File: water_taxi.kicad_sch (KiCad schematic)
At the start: 28 parts

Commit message: pier 50 routing checkpoint
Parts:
- removed LED538, LED587: WS2812B-2020, EasyEDA:LED-SMD_4P-L2.0-W2.0-TL_WS2812B-2020, symbol EasyEDA:WS2812B-2020
- added LED596, LED597, LED598, LED599: WS2812B-2020, EasyEDA:LED-SMD_4P-L2.0-W2.0-TL_WS2812B-2020, symbol EasyEDA:WS2812B-2020
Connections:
- net +VLED: now also LED596.4 (VDD), LED597.4 (VDD), LED598.4 (VDD), LED599.4 (VDD)
- net GND: now also LED596.2 (GND), LED597.2 (GND), LED598.2 (GND), LED599.2 (GND)
- net at LED539.3 (DI): now also LED537.1 (DO)
- net at LED588.3 (DI): now also LED586.1 (DO)
- net at LED593.1 (DO): now also LED598.3 (DI)
- net at LED593.3 (DI): now also LED599.1 (DO); no longer LED591.1 (DO)
- net at LED532.3 (DI): now also LED596.1 (DO)
- net at LED594.1 (DO): now also LED597.3 (DI)
- new net: LED591.1 (DO), LED599.3 (DI)
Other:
- moved on the sheet: LED532, LED534, LED535, LED536, LED537, LED539, LED540, LED541, LED542, LED543, LED544, LED545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

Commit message: single ferry track checkpoint
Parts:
- removed LED582, LED583, LED584, LED585, LED586, LED588, LED589, LED590, LED591, LED592, LED593, LED594, LED597, LED598, LED599: WS2812B-2020, EasyEDA:LED-SMD_4P-L2.0-W2.0-TL_WS2812B-2020, symbol EasyEDA:WS2812B-2020
- added LED538, LED553: WS2812B-2020, EasyEDA:LED-SMD_4P-L2.0-W2.0-TL_WS2812B-2020, symbol EasyEDA:WS2812B-2020
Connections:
- net +VLED: now also LED538.4 (VDD), LED553.4 (VDD)
- net GND: now also LED538.2 (GND), LED553.2 (GND)
- net at LED545.1 (DO): now also LED553.3 (DI); no longer LED546.3 (DI)
- net at LED534.3 (DI): now also LED538.1 (DO); no longer LED532.1 (DO)
- new net: LED546.3 (DI), LED553.1 (DO)
- new net: LED532.1 (DO), LED538.3 (DI)
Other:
- moved on the sheet: LED534, LED535, LED536, LED537

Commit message: checkpoint before label plugin
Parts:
- added LED554: WS2812B-2020, EasyEDA:LED-SMD_4P-L2.0-W2.0-TL_WS2812B-2020, symbol EasyEDA:WS2812B-2020
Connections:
- net +VLED: now also LED554.4 (VDD)
- net GND: now also LED554.2 (GND)
- net at LED544.4 (DIN): now also LED554.1 (DO); no longer LED543.1 (DO)
- new net: LED543.1 (DO), LED554.3 (DI)

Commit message: Add rail labels
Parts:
- renumbered LED596 to LED501, LED532 to LED502, LED538 to LED503, LED534 to LED504, LED535 to LED505, LED536 to LED506, LED537 to LED507, LED539 to LED508, LED540 to LED509, LED541 to LED510, LED542 to LED511, LED543 to LED512, LED554 to LED513, LED544 to LED514, LED545 to LED515, LED553 to LED516, LED546 to LED517, LED547 to LED518
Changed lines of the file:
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@@
 		(in_pos_files yes)
 		(dnp no)
-		(property "Reference" "LED554"
+		(property "Reference" "LED513"
 			(at 267.97 34.544 0)
 			(show_name no)
@@
 			(project "transit"
 				(path "/3763eade-a8c8-4ec0-9cf2-9db4442b4ee5/153adc6e-a3b0-4527-a19a-87e28aab4b4d/f90621d2-7226-466f-89f1-cc8a4ff4cef7"
-					(reference "LED554")
+					(reference "LED513")
 					(unit 1)
 				)
@@
 		(in_pos_files yes)
 		(dnp no)
-		(property "Reference" "LED545"
+		(property "Reference" "LED515"
 			(at 58.42 61.214 0)
 			(show_name no)
@@
 			(project "transit"
 				(path "/3763eade-a8c8-4ec0-9cf2-9db4442b4ee5/153adc6e-a3b0-4527-a19a-87e28aab4b4d/f90621d2-7226-466f-89f1-cc8a4ff4cef7"
-					(reference "LED545")
+					(reference "LED515")
 					(unit 1)
 				)
@@
 		(in_pos_files yes)
 		(dnp no)
-		(property "Reference" "LED546"
+		(property "Reference" "LED517"
 			(at 109.22 61.214 0)
 			(show_name no)
@@
 			(project "transit"
 				(path "/3763eade-a8c8-4ec0-9cf2-9db4442b4ee5/153adc6e-a3b0-4527-a19a-87e28aab4b4d/f90621d2-7226-466f-89f1-cc8a4ff4cef7"
-					(reference "LED546")
+					(reference "LED517")
 					(unit 1)
 				)
@@
 		(in_pos_files yes)
 		(dnp no)
-		(property "Reference" "LED539"
+		(property "Reference" "LED508"
 			(at 170.18 34.544 0)
 			(show_name no)
@@
 			(project "transit"
 				(path "/3763eade-a8c8-4ec0-9cf2-9db4442b4ee5/153adc6e-a3b0-4527-a19a-87e28aab4b4d/f90621d2-7226-466f-89f1-cc8a4ff4cef7"
-					(reference "LED539")
+					(reference "LED508")
 					(unit 1)
 				)
@@
 		(in_pos_files yes)
 		(dnp no)
-		(property "Reference" "LED596"
+		(property "Reference" "LED501"
 			(at 34.29 34.544 0)
 			(show_name no)
@@
 			(project "transit"
 				(path "/3763eade-a8c8-4ec0-9cf2-9db4442b4ee5/153adc6e-a3b0-4527-a19a-87e28aab4b4d/f90621d2-7226-466f-89f1-cc8a4ff4cef7"
-					(reference "LED596")
+					(reference "LED501")
 					(unit 1)
 				)
@@
 		(in_pos_files yes)
 		(dnp no)
-		(property "Reference" "LED534"
+		(property "Reference" "LED504"
 			(at 92.71 34.544 0)
 			(show_name no)
@@
 			(project "transit"
 				(path "/3763eade-a8c8-4ec0-9cf2-9db4442b4ee5/153adc6e-a3b0-4527-a19a-87e28aab4b4d/f90621d2-7226-466f-89f1-cc8a4ff4cef7"
-					(reference "LED534")
+					(reference "LED504")
 					(unit 1)
 				)
@@
 		(in_pos_files yes)
 		(dnp no)
-		(property "Reference" "LED538"
+		(property "Reference" "LED503"
 			(at 73.66 34.544 0)
 			(show_name no)
@@
 			(project "transit"
 				(path "/3763eade-a8c8-4ec0-9cf2-9db4442b4ee5/153adc6e-a3b0-4527-a19a-87e28aab4b4d/f90621d2-7226-466f-89f1-cc8a4ff4cef7"
-					(reference "LED538")
+					(reference "LED503")
 					(unit 1)
 				)
@@
 		(in_pos_files yes)
 		(dnp no)
-		(property "Reference" "LED535"
+		(property "Reference" "LED505"
 			(at 111.76 34.544 0)
 			(show_name no)
@@
 			(project "transit"
 				(path "/3763eade-a8c8-4ec0-9cf2-9db4442b4ee5/153adc6e-a3b0-4527-a19a-87e28aab4b4d/f90621d2-7226-466f-89f1-cc8a4ff4cef7"
-					(reference "LED535")
+					(reference "LED505")
 					(unit 1)
 				)
@@
 		(in_pos_files yes)
 		(dnp no)
-		(property "Reference" "LED536"
+		(property "Reference" "LED506"
 			(at 130.81 34.544 0)
 			(show_name no)
@@
 			(project "transit"
 				(path "/3763eade-a8c8-4ec0-9cf2-9db4442b4ee5/153adc6e-a3b0-4527-a19a-87e28aab4b4d/f90621d2-7226-466f-89f1-cc8a4ff4cef7"
-					(reference "LED536")
+					(reference "LED506")
 					(unit 1)
 				)
@@
 		(in_pos_files yes)
 		(dnp no)
-		(property "Reference" "LED553"
+		(property "Reference" "LED516"
 			(at 82.55 61.214 0)
 			(show_name no)
@@
 			(project "transit"
 				(path "/3763eade-a8c8-4ec0-9cf2-9db4442b4ee5/153adc6e-a3b0-4527-a19a-87e28aab4b4d/f90621d2-7226-466f-89f1-cc8a4ff4cef7"
-					(reference "LED553")
+					(reference "LED516")
 					(unit 1)
 				)
@@
 		(in_pos_files yes)
 		(dnp no)
-		(property "Reference" "LED542"
+		(property "Reference" "LED511"
 			(at 227.33 34.544 0)
 			(show_name no)
@@
 			(project "transit"
 				(path "/3763eade-a8c8-4ec0-9cf2-9db4442b4ee5/153adc6e-a3b0-4527-a19a-87e28aab4b4d/f90621d2-7226-466f-89f1-cc8a4ff4cef7"
-					(reference "LED542")
+					(reference "LED511")
 					(unit 1)
 				)
@@
 		(in_pos_files yes)
 		(dnp no)
-		(property "Reference" "LED544"
+		(property "Reference" "LED514"
 			(at 33.02 58.166 0)
 			(show_name no)
@@
 			(project "transit"
 				(path "/3763eade-a8c8-4ec0-9cf2-9db4442b4ee5/153adc6e-a3b0-4527-a19a-87e28aab4b4d/f90621d2-7226-466f-89f1-cc8a4ff4cef7"
-					(reference "LED544")
+					(reference "LED514")
 					(unit 1)
 				)
@@
 		(in_pos_files yes)
 		(dnp no)
-		(property "Reference" "LED532"
+		(property "Reference" "LED502"
 			(at 54.61 34.544 0)
 			(show_name no)
@@
 			(project "transit"
 				(path "/3763eade-a8c8-4ec0-9cf2-9db4442b4ee5/153adc6e-a3b0-4527-a19a-87e28aab4b4d/f90621d2-7226-466f-89f1-cc8a4ff4cef7"
-					(reference "LED532")
+					(reference "LED502")
 					(unit 1)
 				)
@@
 		(in_pos_files yes)
 		(dnp no)
-		(property "Reference" "LED540"
+		(property "Reference" "LED509"
 			(at 189.23 34.544 0)
 			(show_name no)
@@
 			(project "transit"
 				(path "/3763eade-a8c8-4ec0-9cf2-9db4442b4ee5/153adc6e-a3b0-4527-a19a-87e28aab4b4d/f90621d2-7226-466f-89f1-cc8a4ff4cef7"
-					(reference "LED540")
+					(reference "LED509")
 					(unit 1)
 				)
@@
 		(in_pos_files yes)
 		(dnp no)
-		(property "Reference" "LED541"
+		(property "Reference" "LED510"
 			(at 208.28 34.544 0)
 			(show_name no)
@@
 			(project "transit"
 				(path "/3763eade-a8c8-4ec0-9cf2-9db4442b4ee5/153adc6e-a3b0-4527-a19a-87e28aab4b4d/f90621d2-7226-466f-89f1-cc8a4ff4cef7"
-					(reference "LED541")
+					(reference "LED510")
 					(unit 1)
 				)
@@
 		(in_pos_files yes)
 		(dnp no)
-		(property "Reference" "LED547"
+		(property "Reference" "LED518"
 			(at 132.08 58.166 0)
 			(show_name no)
@@
 			(project "transit"
 				(path "/3763eade-a8c8-4ec0-9cf2-9db4442b4ee5/153adc6e-a3b0-4527-a19a-87e28aab4b4d/f90621d2-7226-466f-89f1-cc8a4ff4cef7"
-					(reference "LED547")
+					(reference "LED518")
 					(unit 1)
 				)
@@
 		(in_pos_files yes)
 		(dnp no)
-		(property "Reference" "LED537"
+		(property "Reference" "LED507"
 			(at 149.86 34.544 0)
 			(show_name no)
@@
 			(project "transit"
 				(path "/3763eade-a8c8-4ec0-9cf2-9db4442b4ee5/153adc6e-a3b0-4527-a19a-87e28aab4b4d/f90621d2-7226-466f-89f1-cc8a4ff4cef7"
-					(reference "LED537")
+					(reference "LED507")
 					(unit 1)
 				)
@@
 		(in_pos_files yes)
 		(dnp no)
-		(property "Reference" "LED543"
+		(property "Reference" "LED512"
 			(at 246.38 34.544 0)
 			(show_name no)
@@
 			(project "transit"
 				(path "/3763eade-a8c8-4ec0-9cf2-9db4442b4ee5/153adc6e-a3b0-4527-a19a-87e28aab4b4d/f90621d2-7226-466f-89f1-cc8a4ff4cef7"
-					(reference "LED543")
+					(reference "LED512")
 					(unit 1)
 				)

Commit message: checkpoint
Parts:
- added LED507: WS2812B-2020, EasyEDA:LED-SMD_4P-L2.0-W2.0-TL_WS2812B-2020, symbol EasyEDA:WS2812B-2020
- renumbered LED507 to LED508, LED508 to LED509, LED509 to LED510, LED510 to LED511, LED511 to LED512, LED512 to LED513, LED513 to LED514, LED514 to LED515, LED515 to LED516, LED516 to LED517, LED517 to LED518, LED518 to LED519
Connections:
- net +VLED: now also LED507.4 (VDD)
- net GND: now also LED507.2 (GND)
- net at LED506.1 (DO): now also LED507.3 (DI); no longer LED508.3 (DI)
- new net: LED507.1 (DO), LED508.3 (DI)
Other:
- moved on the sheet: LED501, LED502, LED503, LED504, LED505, LED506, LED508, LED509, LED510, LED511, LED512, LED513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

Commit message: junction checkpoint
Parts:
- removed LED501: WS2812B-2020, EasyEDA:LED-SMD_4P-L2.0-W2.0-TL_WS2812B-2020, symbol EasyEDA:WS2812B-2020
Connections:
- net +VLED: now also LED502.4 (VDD)
- net at LED515.4 (DIN): now also LED502.3 (DI); no longer LED514.1 (DO)
- net WATER_TAXI_SOUTHWORTH: now reaches LED519.2 (DOUT)
- new net FVS_SEATTLE: LED514.1 (DO)
- no-connect marks 1 -> 0
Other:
- moved on the sheet: LED502, LED503, LED504, LED505, LED506, LED507, LED508, LED509, LED510, LED511, LED512, LED513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

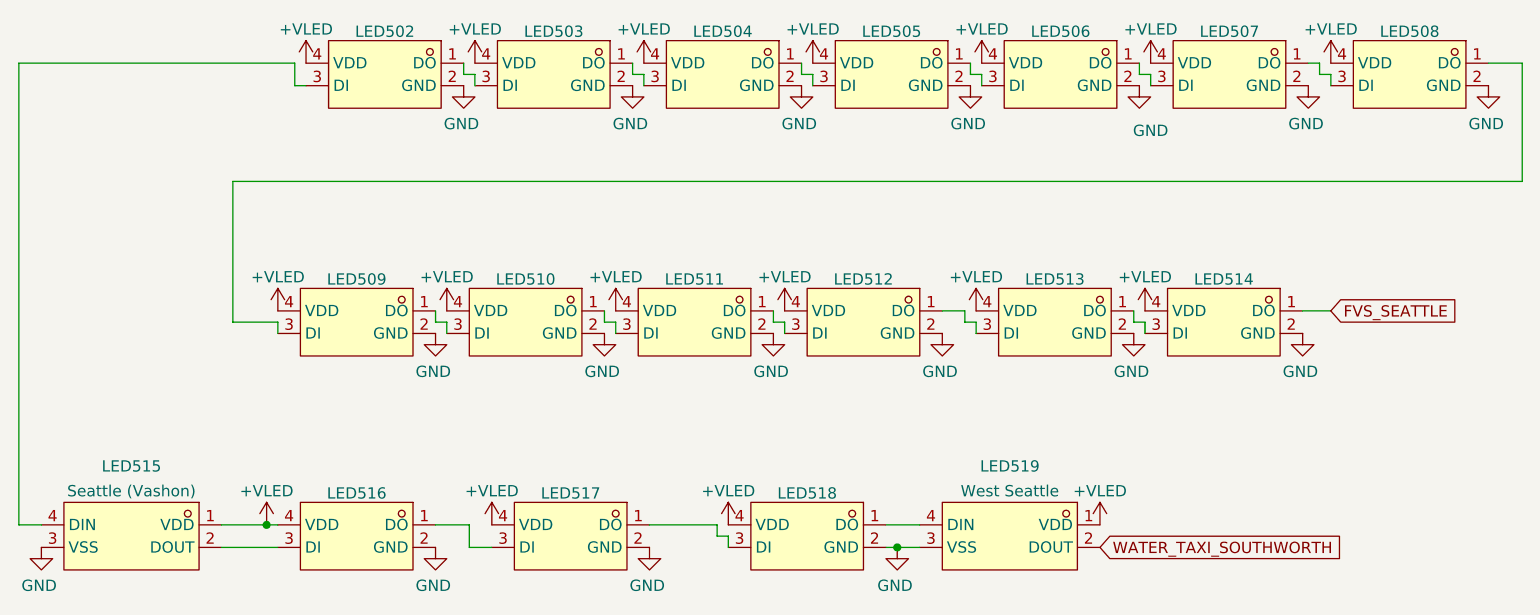
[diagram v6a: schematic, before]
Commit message: reflow reference designators
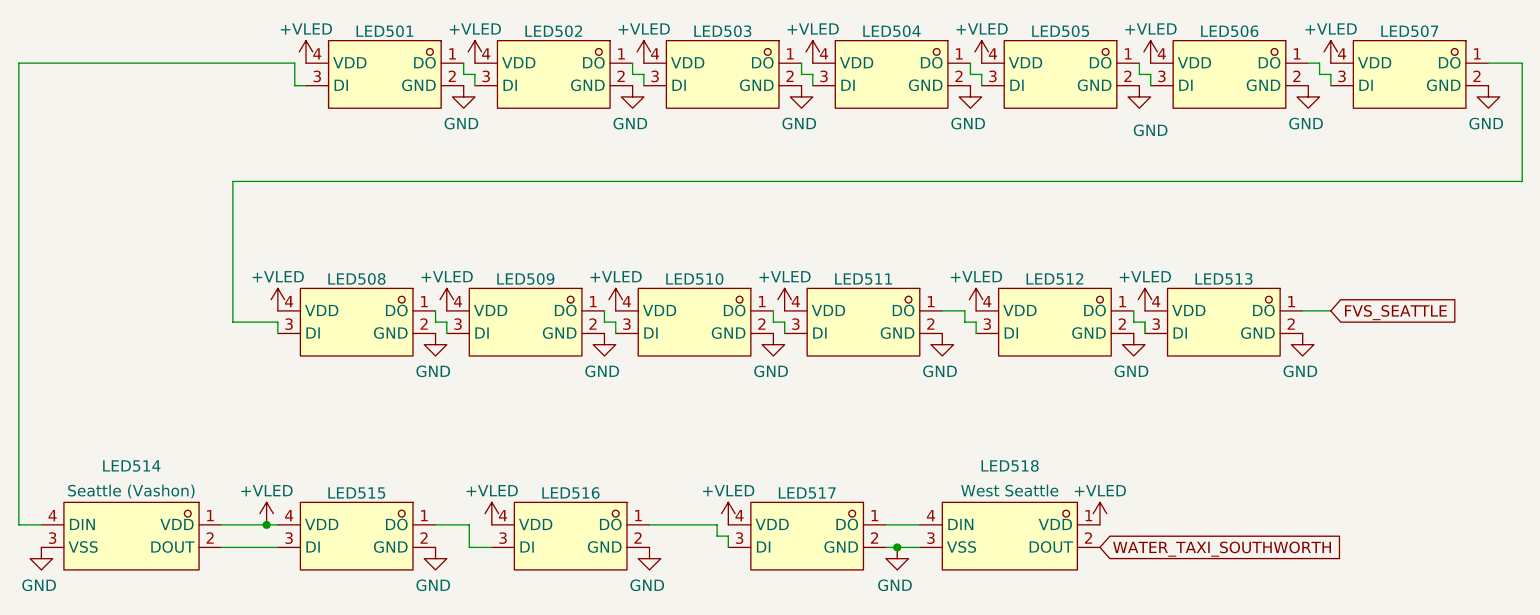
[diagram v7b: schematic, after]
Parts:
- renumbered LED502 to LED501, LED503 to LED502, LED504 to LED503, LED505 to LED504, LED506 to LED505, LED507 to LED506, LED508 to LED507, LED509 to LED508, LED510 to LED509, LED511 to LED510, LED512 to LED511, LED513 to LED512, LED514 to LED513, LED515 to LED514, LED516 to LED515, LED517 to LED516, LED518 to LED517, LED519 to LED518
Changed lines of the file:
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@@
 		(in_pos_files yes)
 		(dnp no)
-		(property "Reference" "LED514"
+		(property "Reference" "LED513"
 			(at 161.29 118.999 0)
 			(show_name no)
@@
 			(project "transit"
 				(path "/3763eade-a8c8-4ec0-9cf2-9db4442b4ee5/153adc6e-a3b0-4527-a19a-87e28aab4b4d/f90621d2-7226-466f-89f1-cc8a4ff4cef7"
-					(reference "LED514")
+					(reference "LED513")
 					(unit 1)
 				)
@@
 		(in_pos_files yes)
 		(dnp no)
-		(property "Reference" "LED516"
+		(property "Reference" "LED515"
 			(at 63.5 143.129 0)
 			(show_name no)
@@
 			(project "transit"
 				(path "/3763eade-a8c8-4ec0-9cf2-9db4442b4ee5/153adc6e-a3b0-4527-a19a-87e28aab4b4d/f90621d2-7226-466f-89f1-cc8a4ff4cef7"
-					(reference "LED516")
+					(reference "LED515")
 					(unit 1)
 				)
@@
 		(in_pos_files yes)
 		(dnp no)
-		(property "Reference" "LED518"
+		(property "Reference" "LED517"
 			(at 114.3 143.129 0)
 			(show_name no)
@@
 			(project "transit"
 				(path "/3763eade-a8c8-4ec0-9cf2-9db4442b4ee5/153adc6e-a3b0-4527-a19a-87e28aab4b4d/f90621d2-7226-466f-89f1-cc8a4ff4cef7"
-					(reference "LED518")
+					(reference "LED517")
 					(unit 1)
 				)
@@
 		(in_pos_files yes)
 		(dnp no)
-		(property "Reference" "LED509"
+		(property "Reference" "LED508"
 			(at 63.5 118.999 0)
 			(show_name no)
@@
 			(project "transit"
 				(path "/3763eade-a8c8-4ec0-9cf2-9db4442b4ee5/153adc6e-a3b0-4527-a19a-87e28aab4b4d/f90621d2-7226-466f-89f1-cc8a4ff4cef7"
-					(reference "LED509")
+					(reference "LED508")
 					(unit 1)
 				)
@@
 		(in_pos_files yes)
 		(dnp no)
-		(property "Reference" "LED504"
+		(property "Reference" "LED503"
 			(at 104.775 91.059 0)
 			(show_name no)
@@
 			(project "transit"
 				(path "/3763eade-a8c8-4ec0-9cf2-9db4442b4ee5/153adc6e-a3b0-4527-a19a-87e28aab4b4d/f90621d2-7226-466f-89f1-cc8a4ff4cef7"
-					(reference "LED504")
+					(reference "LED503")
 					(unit 1)
 				)
@@
 		(in_pos_files yes)
 		(dnp no)
-		(property "Reference" "LED503"
+		(property "Reference" "LED502"
 			(at 85.725 91.059 0)
 			(show_name no)
@@
 			(project "transit"
 				(path "/3763eade-a8c8-4ec0-9cf2-9db4442b4ee5/153adc6e-a3b0-4527-a19a-87e28aab4b4d/f90621d2-7226-466f-89f1-cc8a4ff4cef7"
-					(reference "LED503")
+					(reference "LED502")
 					(unit 1)
 				)
@@
 		(in_pos_files yes)
 		(dnp no)
-		(property "Reference" "LED505"
+		(property "Reference" "LED504"
 			(at 123.825 91.059 0)
 			(show_name no)
@@
 			(project "transit"
 				(path "/3763eade-a8c8-4ec0-9cf2-9db4442b4ee5/153adc6e-a3b0-4527-a19a-87e28aab4b4d/f90621d2-7226-466f-89f1-cc8a4ff4cef7"
-					(reference "LED505")
+					(reference "LED504")
 					(unit 1)
 				)
@@
 		(in_pos_files yes)
 		(dnp no)
-		(property "Reference" "LED506"
+		(property "Reference" "LED505"
 			(at 142.875 91.059 0)
 			(show_name no)
@@
 			(project "transit"
 				(path "/3763eade-a8c8-4ec0-9cf2-9db4442b4ee5/153adc6e-a3b0-4527-a19a-87e28aab4b4d/f90621d2-7226-466f-89f1-cc8a4ff4cef7"
-					(reference "LED506")
+					(reference "LED505")
 					(unit 1)
 				)
@@
 		(in_pos_files yes)
 		(dnp no)
-		(property "Reference" "LED517"
+		(property "Reference" "LED516"
 			(at 87.63 143.129 0)
 			(show_name no)
@@
 			(project "transit"
 				(path "/3763eade-a8c8-4ec0-9cf2-9db4442b4ee5/153adc6e-a3b0-4527-a19a-87e28aab4b4d/f90621d2-7226-466f-89f1-cc8a4ff4cef7"
-					(reference "LED517")
+					(reference "LED516")
 					(unit 1)
 				)
@@
 		(in_pos_files yes)
 		(dnp no)
-		(property "Reference" "LED512"
+		(property "Reference" "LED511"
 			(at 120.65 118.999 0)
 			(show_name no)
@@
 			(project "transit"
 				(path "/3763eade-a8c8-4ec0-9cf2-9db4442b4ee5/153adc6e-a3b0-4527-a19a-87e28aab4b4d/f90621d2-7226-466f-89f1-cc8a4ff4cef7"
-					(reference "LED512")
+					(reference "LED511")
 					(unit 1)
 				)
@@
 		(in_pos_files yes)
 		(dnp no)
-		(property "Reference" "LED515"
+		(property "Reference" "LED514"
 			(at 38.1 140.081 0)
 			(show_name no)
@@
 			(project "transit"
 				(path "/3763eade-a8c8-4ec0-9cf2-9db4442b4ee5/153adc6e-a3b0-4527-a19a-87e28aab4b4d/f90621d2-7226-466f-89f1-cc8a4ff4cef7"
-					(reference "LED515")
+					(reference "LED514")
 					(unit 1)
 				)
@@
 		(in_pos_files yes)
 		(dnp no)
-		(property "Reference" "LED507"
+		(property "Reference" "LED506"
 			(at 161.925 91.059 0)
 			(show_name no)
@@
 			(project "transit"
 				(path "/3763eade-a8c8-4ec0-9cf2-9db4442b4ee5/153adc6e-a3b0-4527-a19a-87e28aab4b4d/f90621d2-7226-466f-89f1-cc8a4ff4cef7"
-					(reference "LED507")
+					(reference "LED506")
 					(unit 1)
 				)
@@
 		(in_pos_files yes)
 		(dnp no)
-		(property "Reference" "LED502"
+		(property "Reference" "LED501"
 			(at 66.675 91.059 0)
 			(show_name no)
@@
 			(project "transit"
 				(path "/3763eade-a8c8-4ec0-9cf2-9db4442b4ee5/153adc6e-a3b0-4527-a19a-87e28aab4b4d/f90621d2-7226-466f-89f1-cc8a4ff4cef7"
-					(reference "LED502")
+					(reference "LED501")
 					(unit 1)
 				)
@@
 		(in_pos_files yes)
 		(dnp no)
-		(property "Reference" "LED510"
+		(property "Reference" "LED509"
 			(at 82.55 118.999 0)
 			(show_name no)
@@
 			(project "transit"
 				(path "/3763eade-a8c8-4ec0-9cf2-9db4442b4ee5/153adc6e-a3b0-4527-a19a-87e28aab4b4d/f90621d2-7226-466f-89f1-cc8a4ff4cef7"
-					(reference "LED510")
+					(reference "LED509")
 					(unit 1)
 				)
@@
 		(in_pos_files yes)
 		(dnp no)
-		(property "Reference" "LED511"
+		(property "Reference" "LED510"
 			(at 101.6 118.999 0)
 			(show_name no)
@@
 			(project "transit"
 				(path "/3763eade-a8c8-4ec0-9cf2-9db4442b4ee5/153adc6e-a3b0-4527-a19a-87e28aab4b4d/f90621d2-7226-466f-89f1-cc8a4ff4cef7"
-					(reference "LED511")
+					(reference "LED510")
 					(unit 1)
 				)
@@
 		(in_pos_files yes)
 		(dnp no)
-		(property "Reference" "LED519"
+		(property "Reference" "LED518"
 			(at 137.16 140.081 0)
 			(show_name no)
@@
 			(project "transit"
 				(path "/3763eade-a8c8-4ec0-9cf2-9db4442b4ee5/153adc6e-a3b0-4527-a19a-87e28aab4b4d/f90621d2-7226-466f-89f1-cc8a4ff4cef7"
-					(reference "LED519")
+					(reference "LED518")
 					(unit 1)
 				)
@@
 		(in_pos_files yes)
 		(dnp no)
-		(property "Reference" "LED508"
+		(property "Reference" "LED507"
 			(at 182.245 91.059 0)
 			(show_name no)
@@
 			(project "transit"
 				(path "/3763eade-a8c8-4ec0-9cf2-9db4442b4ee5/153adc6e-a3b0-4527-a19a-87e28aab4b4d/f90621d2-7226-466f-89f1-cc8a4ff4cef7"
-					(reference "LED508")
+					(reference "LED507")
 					(unit 1)
 				)
@@
 		(in_pos_files yes)
 		(dnp no)
-		(property "Reference" "LED513"
+		(property "Reference" "LED512"
 			(at 142.24 118.999 0)
 			(show_name no)
@@
 			(project "transit"
 				(path "/3763eade-a8c8-4ec0-9cf2-9db4442b4ee5/153adc6e-a3b0-4527-a19a-87e28aab4b4d/f90621d2-7226-466f-89f1-cc8a4ff4cef7"
-					(reference "LED513")
+					(reference "LED512")
 					(unit 1)
 				)

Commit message: rev-b validation run
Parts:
- LED501, LED502, LED503, LED504, LED505, LED506, LED507, LED508, LED509, LED510, LED511, LED512, LED513, LED515, LED516, LED517: LCSC Part C965555 -> C52917434
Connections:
- net FVS_SEATTLE: now also LED501.3 (DI); no longer LED513.1 (DO)
- net at LED514.4 (DIN): now also LED513.1 (DO); no longer LED501.3 (DI)
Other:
- moved on the sheet: LED514, LED515, LED516, LED517, LED518
